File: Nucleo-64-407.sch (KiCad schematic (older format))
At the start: 57 parts, among them J1 SWD, J2 Micro_SD_Card_Det, J3 USB_B_Micro, J4 Serial 0, J5 EXP1, J6 EXP2, J7 EXP3, J8 EXP4, SW1 RESET, SW2 BOOT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

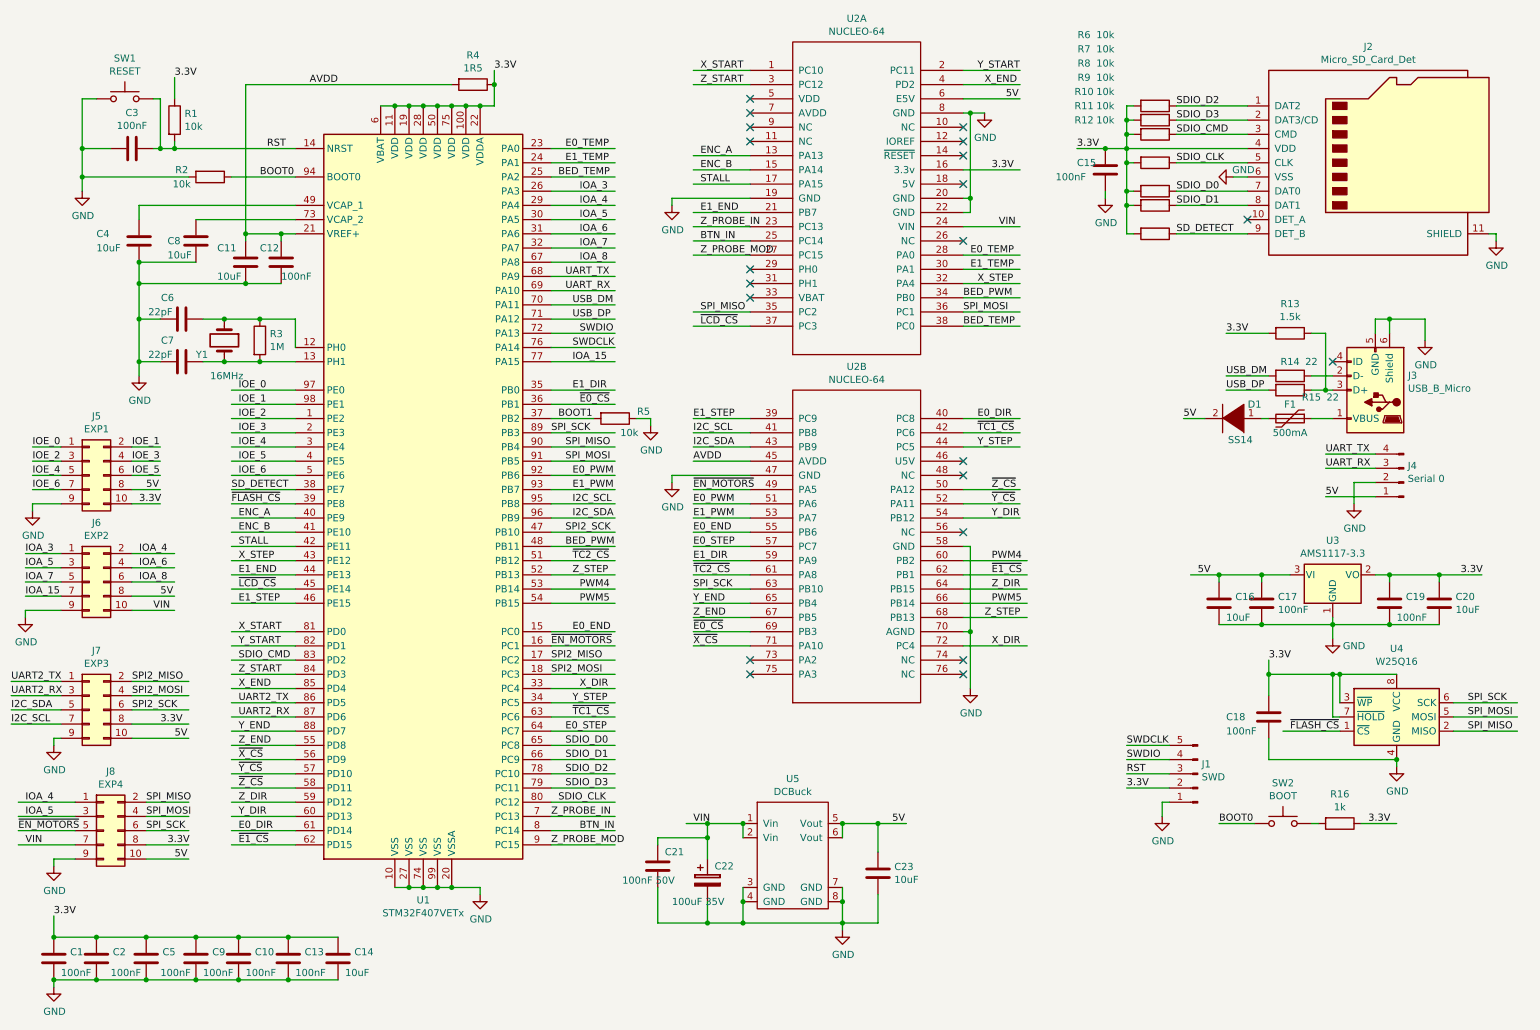
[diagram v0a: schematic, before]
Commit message: Routed NUCLEO-64-F407
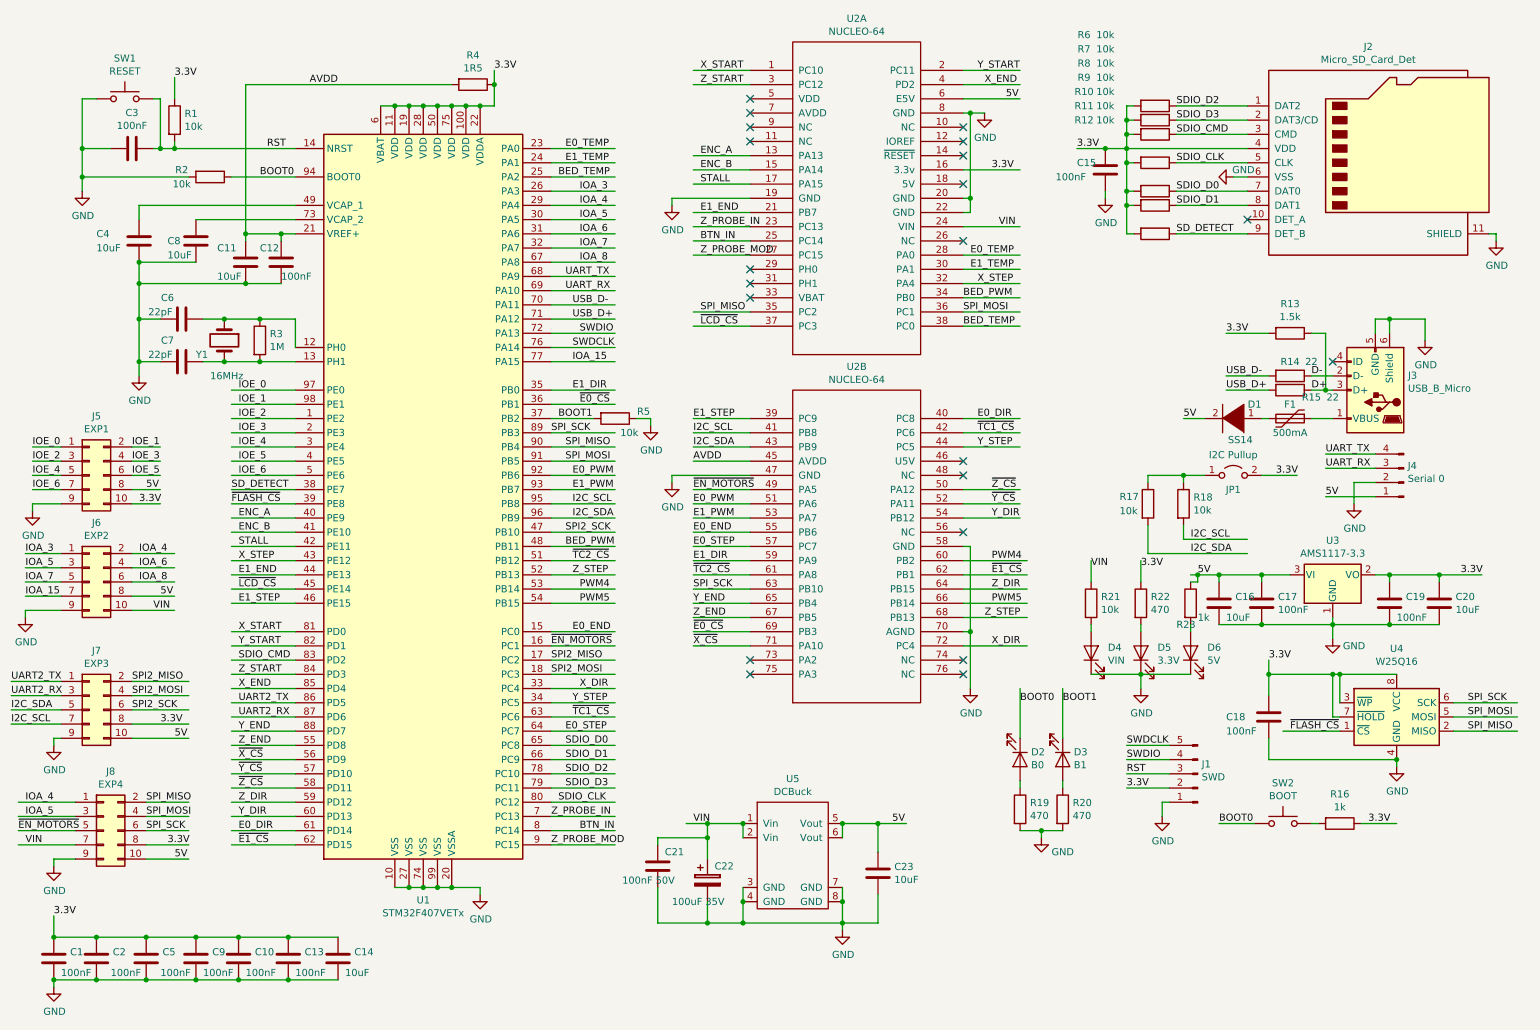
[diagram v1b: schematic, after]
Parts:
- added D2: B0, PrntrBoardV1:D_0603_1608Metric, symbol Device:LED
- added D3: B1, PrntrBoardV1:D_0603_1608Metric, symbol Device:LED
- added D4: VIN, PrntrBoardV1:D_0603_1608Metric, symbol Device:LED
- added D5: 3.3V, PrntrBoardV1:D_0603_1608Metric, symbol Device:LED
- added D6: 5V, PrntrBoardV1:D_0603_1608Metric, symbol Device:LED
- added JP1: I2C Pullup, Jumper:SolderJumper-2_P1.3mm_Open_TrianglePad1.0x1.5mm, symbol Jumper:Jumper_2_Open
- added R17, R18, R21: 10k, PrntrBoardV1:R_0603_1608Metric, symbol Device:R
- added R19, R20, R22: 470, PrntrBoardV1:R_0603_1608Metric, symbol Device:R
- added R23: 1k, PrntrBoardV1:R_0603_1608Metric, symbol Device:R
- C1, C10, C11, C12, C13, C14, C15, C16, C17, C18, C19, C2, C20, C21, C23, C3, C4, C5, C6, C7, C8, C9: footprint (none) -> PrntrBoardV1:C_0603_1608Metric
- C22: footprint (none) -> Capacitor_SMD:CP_Elec_6.3x5.4
- D1: footprint (none) -> Diode_SMD:D_SOD-123F
- F1: footprint (none) -> Fuse:Fuse_0603_1608Metric
- J1: footprint (none) -> Connector_PinHeader_2.54mm:PinHeader_1x05_P2.54mm_Vertical
- J2: footprint (none) -> Connector_Card:microSD_HC_Hirose_DM3AT-SF-PEJM5
- J3: footprint (none) -> Connector_USB:USB_Micro-B_GCT_USB3076-30-A
- J4: footprint (none) -> Connector_PinHeader_2.54mm:PinHeader_1x04_P2.54mm_Vertical
- J5, J6, J7, J8: footprint (none) -> Connector_IDC:IDC-Header_2x05_P2.54mm_Vertical
- R1, R10, R11, R12, R13, R14, R15, R16, R2, R3, R4, R5, R6, R7, R8, R9: footprint (none) -> PrntrBoardV1:R_0603_1608Metric
- SW1, SW2: footprint (none) -> Button_Switch_SMD:SW_SPST_B3SL-1002P
- U2: footprint MODULE -> PrntrBoardV1:Nucleo-64
- U4: footprint (none) -> Package_SO:SO-8_5.3x6.2mm_P1.27mm
- U5: footprint (none) -> DCBuck:Buck2217
- Y1: footprint (none) -> Crystal:Crystal_SMD_HC49-SD
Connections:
- net labels added: D+, D-, USB_D+, USB_D-
- net labels removed: USB_DM, USB_DP
- wire segments 371 -> 398

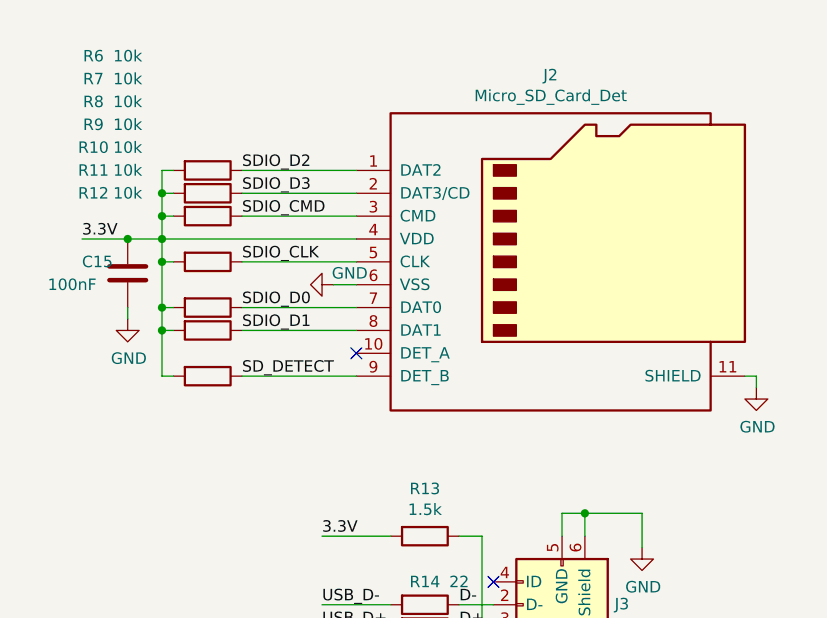
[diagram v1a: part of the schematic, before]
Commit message: Ordered rev1 of the Nucleo-64 board.
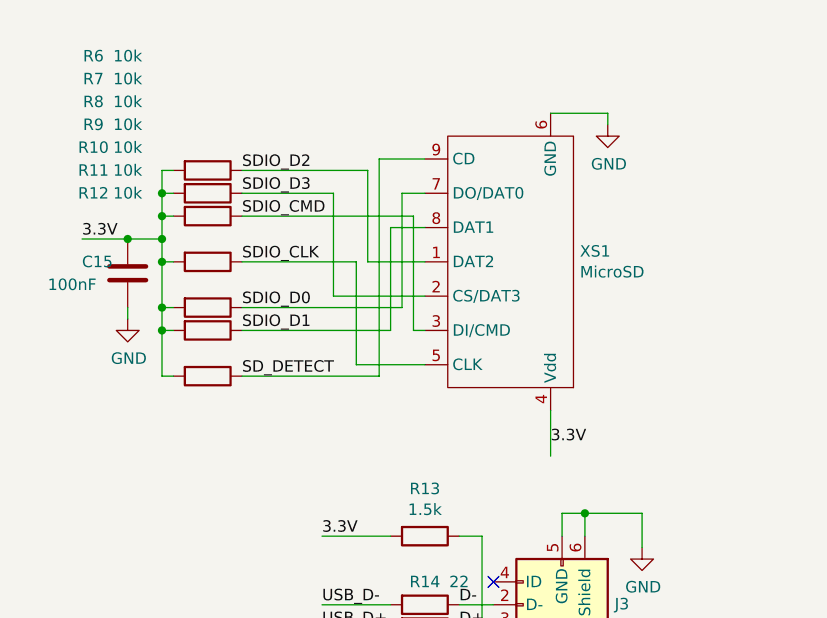
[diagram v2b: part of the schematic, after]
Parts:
- removed J2: Micro_SD_Card_Det, Connector_Card:microSD_HC_Hirose_DM3AT-SF-PEJM5, symbol Connector:Micro_SD_Card_Det
- added XS1: MicroSD, PrntrBoardV1:Conn_uSDcard, symbol uSD_push-push_ebay:SD_ebay-uSD-push_push_SMD
- J3: footprint Connector_USB:USB_Micro-B_GCT_USB3076-30-A -> PrntrBoardV1:MC-101C
- SW1, SW2: footprint Button_Switch_SMD:SW_SPST_B3SL-1002P -> PrntrBoardV1:Button 4x4
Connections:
- wire segments 398 -> 411
- no-connect marks 21 -> 20
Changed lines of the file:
@@
 F 0 "SW1" H 1300 1435 50  0000 C CNN
 F 1 "RESET" H 1300 1344 50  0000 C CNN
-F 2 "Button_Switch_SMD:SW_SPST_B3SL-1002P" H 1300 1350 50  0001 C CNN
+F 2 "PrntrBoardV1:Button 4x4" H 1300 1350 50  0001 C CNN
 F 3 "" H 1300 1350 50  0001 C CNN
 	1    1300 1150
@@
 F 0 "J3" H 9870 3097 50  0000 R CNN
 F 1 "USB_B_Micro" H 9870 3188 50  0000 R CNN
-F 2 "Connector_USB:USB_Micro-B_GCT_USB3076-30-A" H 10250 3150 50  0001 C CNN
+F 2 "PrntrBoardV1:MC-101C" H 10250 3150 50  0001 C CNN
 F 3 "~" H 10250 3150 50  0001 C CNN
 	1    10100 3200
@@
 $EndComp
 Wire Wire Line
-	9200 1900 8700 1900
-Wire Wire Line
-	9200 1800 8700 1800
-Wire Wire Line
 	9200 1600 8700 1600
-Wire Wire Line
-	9200 1400 8700 1400
-Wire Wire Line
-	9200 1300 8700 1300
-Wire Wire Line
-	9200 1200 8700 1200
-Wire Wire Line
-	9200 1500 8350 1500
 Text Label 8000 1500 0    50   ~ 0
 3.3V
@@
 Wire Wire Line
 	8200 1850 8200 1800
-$Comp
-L power:GND #PWR0106
-U 1 1 5BFC0CC7
-P 9100 1700
-F 0 "#PWR0106" H 9100 1450 50  0001 C CNN
-F 1 "GND" V 9050 1850 50  0000 R CNN
-F 2 "" H 9100 1700 50  0001 C CNN
-F 3 "" H 9100 1700 50  0001 C CNN
-	1    9100 1700
-	0    1    1    0
-$EndComp
-Wire Wire Line
-	9100 1700 9200 1700
 $Comp
 L Device:R R12
@@
 L power:GND #PWR0107
 U 1 1 5BFCD156
-P 10950 2150
-F 0 "#PWR0107" H 10950 1900 50  0001 C CNN
-F 1 "GND" H 10955 1977 50  0000 C CNN
-F 2 "" H 10950 2150 50  0001 C CNN
-F 3 "" H 10950 2150 50  0001 C CNN
-	1    10950 2150
-	1    0    0    -1
-$EndComp
-Wire Wire Line
-	10950 2150 10950 2100
-Wire Wire Line
-	10950 2100 10900 2100
-$Comp
-L Connector:Micro_SD_Card_Det J2
-U 1 1 5BFD09A3
-P 10100 1600
-F 0 "J2" H 10050 2417 50  0000 C CNN
-F 1 "Micro_SD_Card_Det" H 10050 2326 50  0000 C CNN
-F 2 "Connector_Card:microSD_HC_Hirose_DM3AT-SF-PEJM5" H 12150 2300 50  0001 C CNN
-F 3 "https://www.hirose.com/product/en/download_file/key_name/DM3/category/Catalog/doc_file_id/49662/?file_category_id=4&item_id=195&is_series=1" H 10100 1700 50  0001 C CNN
-	1    10100 1600
+P 10300 1000
+F 0 "#PWR0107" H 10300 750 50  0001 C CNN
+F 1 "GND" H 10305 827 50  0000 C CNN
+F 2 "" H 10300 1000 50  0001 C CNN
+F 3 "" H 10300 1000 50  0001 C CNN
+	1    10300 1000
 	1    0    0    -1
 $EndComp
@@
 Wire Wire Line
 	8350 1900 8350 2100
-Wire Wire Line
-	9200 2100 8700 2100
-NoConn ~ 9200 2000
-Text Label 8700 2100 0    50   ~ 0
-SD_DETECT
-Text Label 8700 1900 0    50   ~ 0
-SDIO_D1
-Text Label 8700 1800 0    50   ~ 0
-SDIO_D0
-Text Label 8700 1600 0    50   ~ 0
-SDIO_CLK
-Text Label 8700 1400 0    50   ~ 0
-SDIO_CMD
-Text Label 8700 1300 0    50   ~ 0
-SDIO_D3
-Text Label 8700 1200 0    50   ~ 0
-SDIO_D2
 $Comp
 L power:GND #PWR0108
@@
 F 0 "SW2" H 9450 6535 50  0000 C CNN
 F 1 "BOOT" H 9450 6444 50  0000 C CNN
-F 2 "Button_Switch_SMD:SW_SPST_B3SL-1002P" H 9450 6450 50  0001 C CNN
+F 2 "PrntrBoardV1:Button 4x4" H 9450 6450 50  0001 C CNN
 F 3 "" H 9450 6450 50  0001 C CNN
 	1    9450 6250
@@
 Text Label 7900 5400 0    50   ~ 0
 BOOT1
+Wire Wire Line
+	10300 950  10300 1000
+Text Label 10050 2400 0    50   ~ 0
+3.3V
+Wire Wire Line
+	10050 950  10300 950
+Text Label 8700 2100 0    50   ~ 0
+SD_DETECT
+Text Label 8700 1900 0    50   ~ 0
+SDIO_D1
+Text Label 8700 1800 0    50   ~ 0
+SDIO_D0
+Text Label 8700 1600 0    50   ~ 0
+SDIO_CLK
+Text Label 8700 1200 0    50   ~ 0
+SDIO_D2
+Text Label 8700 1300 0    50   ~ 0
+SDIO_D3
+Text Label 8700 1400 0    50   ~ 0
+SDIO_CMD
+$Comp
+L uSD_push-push_ebay:SD_ebay-uSD-push_push_SMD XS1
+U 1 1 5C556F48
+P 9900 1600
+F 0 "XS1" H 9622 1554 50  0000 R CNN
+F 1 "MicroSD" H 9622 1645 50  0000 R CNN
+F 2 "PrntrBoardV1:Conn_uSDcard" H 9900 1600 10  0001 C CNN
+F 3 "_" H 9900 1600 10  0001 C CNN
+F 4 "_" H 9900 1600 10  0001 C CNN "Manf#"
+F 5 "ebay" H 9900 1600 10  0001 C CNN "Manf"
+	1    9900 1600
+	-1   0    0    1
+$EndComp
+Wire Wire Line
+	10050 2250 10050 2450
+Wire Wire Line
+	9300 2100 9300 1150
+Wire Wire Line
+	9300 1150 9500 1150
+Wire Wire Line
+	8700 2100 9300 2100
+Wire Wire Line
+	9500 1900 9450 1900
+Wire Wire Line
+	9450 1900 9450 1400
+Wire Wire Line
+	8700 1400 9450 1400
+Wire Wire Line
+	9400 1800 9400 1300
+Wire Wire Line
+	9400 1300 9500 1300
+Wire Wire Line
+	8700 1800 9400 1800
+Wire Wire Line
+	9500 1450 9350 1450
+Wire Wire Line
+	9350 1450 9350 1900
+Wire Wire Line
+	8700 1900 9350 1900
+Wire Wire Line
+	9500 1600 9250 1600
+Wire Wire Line
+	9250 1600 9250 1200
+Wire Wire Line
+	8700 1200 9250 1200
+Wire Wire Line
+	9500 1750 9100 1750
+Wire Wire Line
+	9100 1750 9100 1300
+Wire Wire Line
+	9100 1300 8700 1300
+Wire Wire Line
+	9200 1600 9200 2050
+Wire Wire Line
+	9200 2050 9500 2050
 $EndSCHEMATC

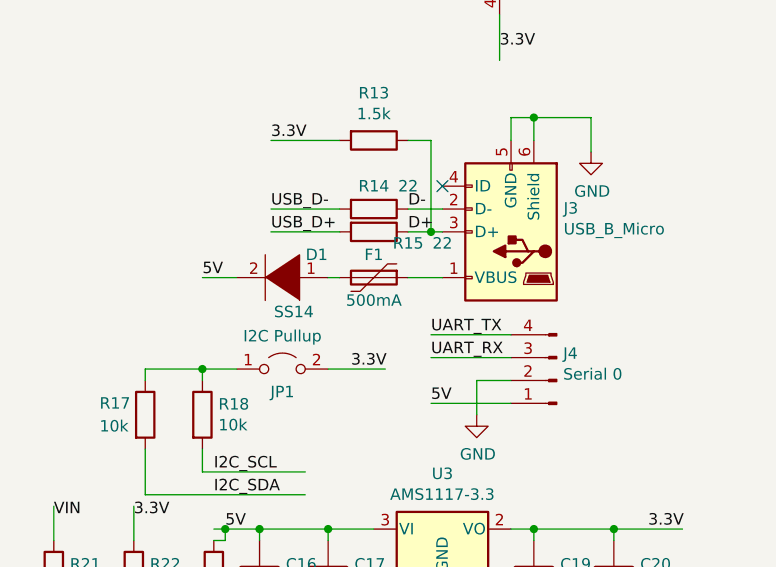
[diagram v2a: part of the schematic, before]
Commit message: Updated EExtruder ground routing. Renamed Nucleo-64 LED values.
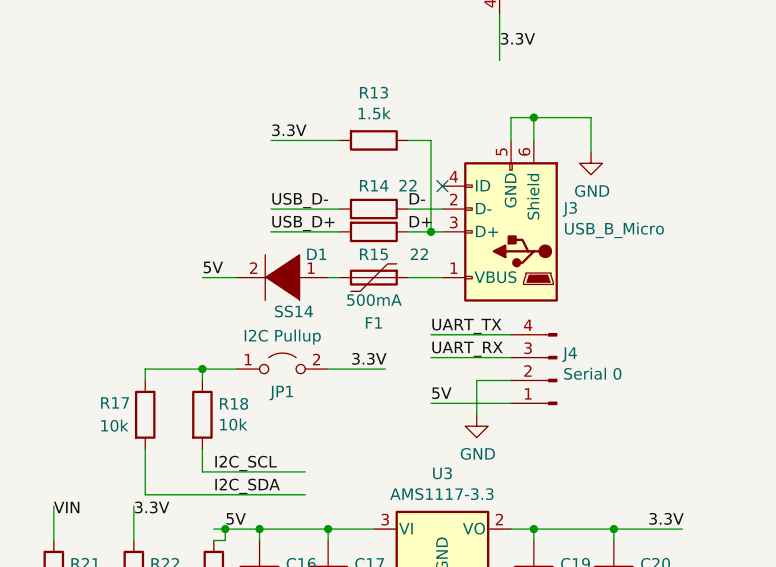
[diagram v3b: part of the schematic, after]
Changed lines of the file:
@@
 U 1 1 5BFEBC2C
 P 9500 3400
-F 0 "F1" V 9400 3400 50  0000 C CNN
+F 0 "F1" V 9700 3400 50  0000 C CNN
 F 1 "500mA" V 9600 3400 50  0000 C CNN
 F 2 "Fuse:Fuse_0603_1608Metric" H 9550 3200 50  0001 L CNN
@@
 U 1 1 5BFF28CB
 P 9500 3200
-F 0 "R15" V 9550 3350 50  0000 C CNN
-F 1 "22" V 9550 3500 50  0000 C CNN
+F 0 "R15" V 9600 3200 50  0000 C CNN
+F 1 "22" V 9600 3400 50  0000 C CNN
 F 2 "PrntrBoardV1:R_0603_1608Metric" V 9430 3200 50  0001 C CNN
 F 3 "~" H 9500 3200 50  0001 C CNN
